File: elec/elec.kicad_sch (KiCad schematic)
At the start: 14 parts, among them J1 BM04B-SRSS-TB, J10 BM04B-SRSS-TB, J11 DB301V-3.5-2P-GN-S, J2 BM04B-SRSS-TB, J3 BM04B-SRSS-TB, J4 BM04B-SRSS-TB, J5 BM04B-SRSS-TB, J6 BM04B-SRSS-TB, J7 BM04B-SRSS-TB, J8 BM04B-SRSS-TB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

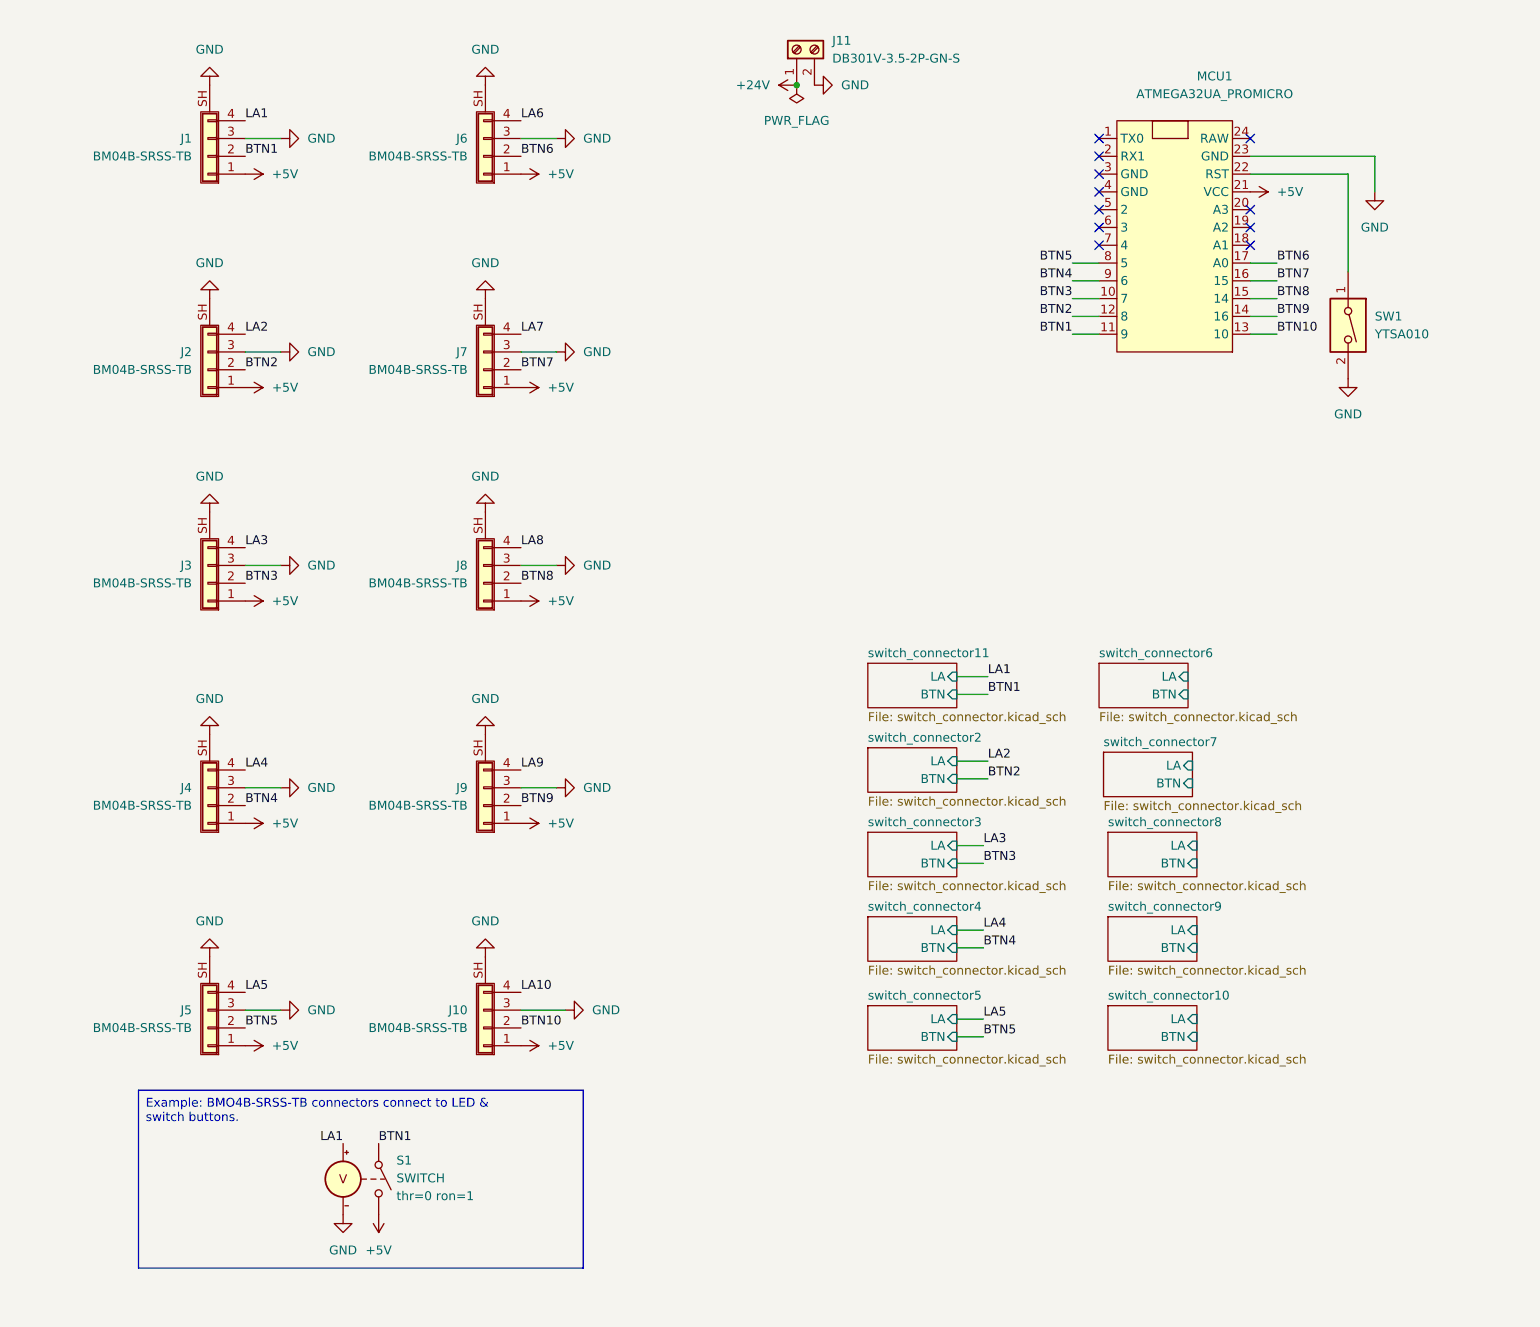
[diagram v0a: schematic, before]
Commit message: feat: adding modularity to PCB
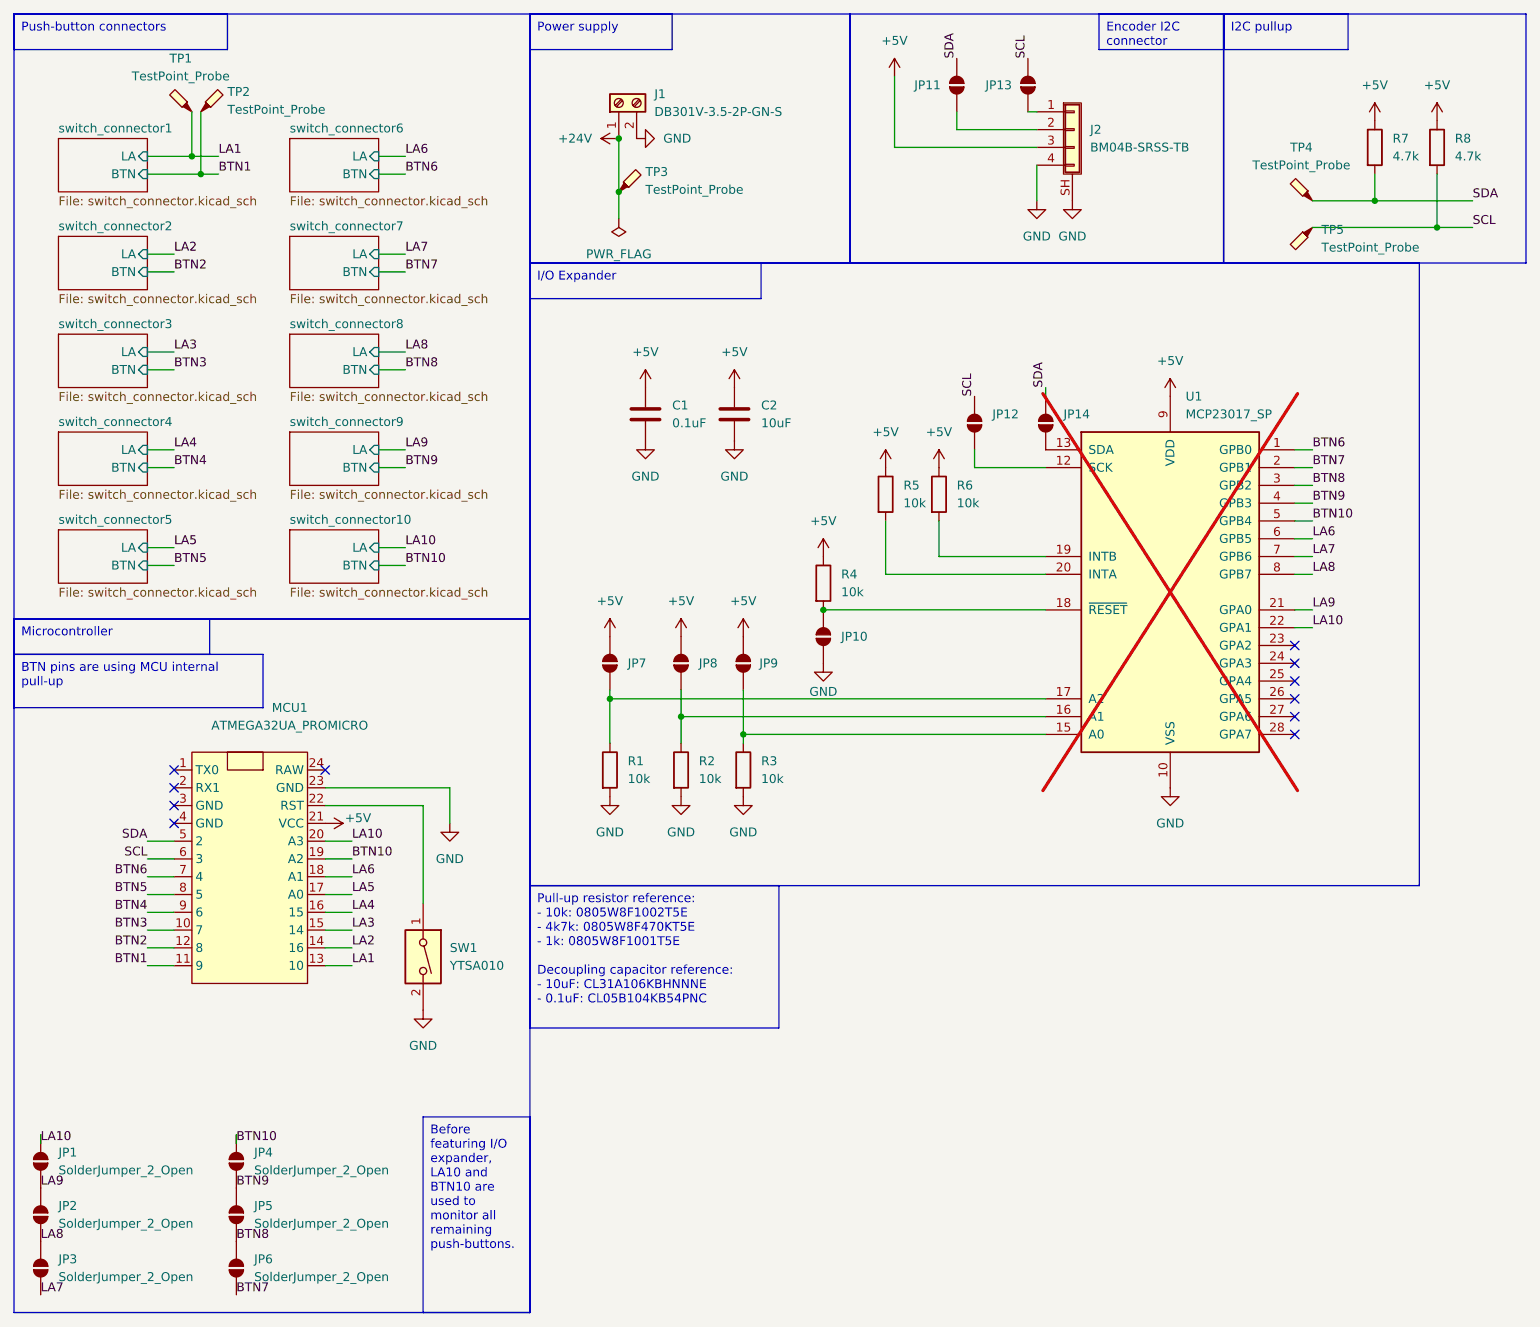
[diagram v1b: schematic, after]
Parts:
- removed J1, J10, J3, J4, J5, J6, J7, J8, J9: BM04B-SRSS-TB, jlcpcb:JST_SH_BM04B-SRSS-TB_1x04-1MP_P1.00mm_Vertical, symbol Connector_Generic_Shielded:Conn_01x04_Shielded
- removed S1: SWITCH, symbol Simulation_SPICE:SWITCH
- added C1: 0.1uF, Capacitor_SMD:C_0402_1005Metric, symbol Device:C
- added C2: 10uF, Capacitor_SMD:C_1206_3216Metric, symbol Device:C
- added JP1, JP10, JP12, JP13, JP14, JP2, JP3, JP4, JP5, JP6, JP7, JP8, JP9: SolderJumper_2_Open, Jumper:SolderJumper-2_P1.3mm_Open_Pad1.0x1.5mm, symbol Jumper:SolderJumper_2_Open
- added JP11: SolderJumper_2_Open, Jumper:SolderJumper-2_P1.3mm_Bridged_Pad1.0x1.5mm, symbol Jumper:SolderJumper_2_Open
- added R1, R2, R3, R4, R5, R6: 10k, Resistor_SMD:R_0805_2012Metric, symbol Device:R
- added R7, R8: 4.7k, Resistor_SMD:R_0805_2012Metric, symbol Device:R
- added TP1, TP2, TP3, TP4, TP5: TestPoint_Probe, TestPoint:TestPoint_THTPad_D3.0mm_Drill1.5mm, symbol Connector:TestPoint_Probe
- added U1: MCP23017_SP, Package_DIP:DIP-28_W7.62mm, symbol Interface_Expansion:MCP23017_SP
- renumbered J11 to J1
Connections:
- net +24V: now also TP3.1
- net +5V: now also J2.3 (Pin_3), C1.1, C2.1, JP7.1 (A), JP8.1 (A), JP9.1 (A), R4.1, R5.1, R6.1, R7.1, R8.1, U1.9 (VDD); no longer J2.1 (Pin_1)
- net BTN1: now also TP2.1
- net BTN10: now also MCU1.19 (A2), JP4.2 (B), U1.5 (GPB4); no longer MCU1.13 (10)
- net BTN2: no longer J2.2 (Pin_2)
- net BTN6: now also MCU1.7 (4), U1.1 (GPB0); no longer MCU1.17 (A0)
- net BTN7: now also JP6.1 (A), U1.2 (GPB1); no longer MCU1.16 (15)
- net BTN8: now also JP5.2 (B), JP6.2 (B), U1.3 (GPB2); no longer MCU1.15 (14)
- net BTN9: now also JP4.1 (A), JP5.1 (A), U1.4 (GPB3); no longer MCU1.14 (16)
- net GND: now also J2.4 (Pin_4), C1.2, C2.2, JP10.1 (A), R1.2, R2.2, R3.2, U1.10 (VSS); no longer J2.3 (Pin_3)
- net LA1: now also MCU1.13 (10), TP1.1
- net LA10: now also MCU1.20 (A3), JP1.2 (B), U1.22 (GPA1)
- net LA2: now also MCU1.14 (16); no longer J2.4 (Pin_4)
- net LA3: now also MCU1.15 (14)
- net LA4: now also MCU1.16 (15)
- net LA5: now also MCU1.17 (A0)
- net LA6: now also MCU1.18 (A1), U1.6 (GPB5)
- net LA7: now also JP3.1 (A), U1.7 (GPB6)
- net LA8: now also JP2.2 (B), JP3.2 (B), U1.8 (GPB7)
- net LA9: now also JP1.1 (A), JP2.1 (A), U1.21 (GPA0)
- net SDA: now reaches MCU1.5 (2)
- net SDA: now also JP11.2 (B), JP14.1 (A), R7.2, TP4.1
- net SCL: now reaches MCU1.6 (3)
- net SCL: now also JP12.2 (B), JP13.2 (B), R8.2, TP5.1
- new net: J2.1 (Pin_1), JP13.1 (A)
- new net: J2.2 (Pin_2), JP11.1 (A)
- new net: JP9.2 (B), R3.1, U1.15 (A0)
- new net: JP10.2 (B), R4.2, U1.18 (~{RESET})
- new net: JP12.1 (A), U1.12 (SCK)
- new net: JP14.2 (B), U1.13 (SDA)
- new net: JP8.2 (B), R2.1, U1.16 (A1)
- new net: JP7.2 (B), R1.1, U1.17 (A2)
- new net: R6.2, U1.19 (INTB)
- new net: R5.2, U1.20 (INTA)
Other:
- removed sheet switch_connector11
- added sheet switch_connector1 (switch_connector.kicad_sch)
- moved on the sheet: J1, MCU1, SW1

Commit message: v1 3D print PCB
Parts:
- renumbered JP6 to JP4, JP4 to JP5, JP5 to JP6
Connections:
- net +24V: now also J1.2 (Pin_2); no longer J1.1 (Pin_1)
- net BTN1: now also MCU1.14 (16); no longer MCU1.11 (9)
- net BTN10: now also MCU1.8 (5), U1.22 (GPA1); no longer MCU1.19 (A2), U1.5 (GPB4)
- net BTN2: now also MCU1.16 (15); no longer MCU1.12 (8)
- net BTN3: now also MCU1.18 (A1); no longer MCU1.10 (7)
- net BTN4: now also MCU1.20 (A3); no longer MCU1.9 (6)
- net BTN5: now also MCU1.11 (9); no longer MCU1.8 (5)
- net BTN6: now also MCU1.10 (7), U1.2 (GPB1); no longer MCU1.7 (4), U1.1 (GPB0)
- net BTN7: now also MCU1.9 (6), U1.28 (GPA7); no longer JP4.1 (A), U1.2 (GPB1)
- net BTN8: now also U1.26 (GPA5); no longer JP4.2 (B), U1.3 (GPB2)
- net BTN9: now also U1.24 (GPA3); no longer U1.4 (GPB3)
- net GND: now also J1.1 (Pin_1), MCU1.3 (GND), MCU1.4 (GND); no longer J1.2 (Pin_2)
- net LA10: now also MCU1.7 (4), U1.21 (GPA0); no longer MCU1.20 (A3), U1.22 (GPA1)
- net LA2: now also MCU1.15 (14); no longer MCU1.14 (16)
- net LA3: now also MCU1.17 (A0); no longer MCU1.15 (14)
- net LA4: now also MCU1.19 (A2); no longer MCU1.16 (15)
- net LA5: now also MCU1.12 (8); no longer MCU1.17 (A0)
- net LA6: now also JP4.1 (A), U1.1 (GPB0); no longer MCU1.18 (A1), U1.6 (GPB5)
- net LA7: now also JP4.2 (B), U1.27 (GPA6); no longer U1.7 (GPB6)
- net LA8: now also U1.25 (GPA4); no longer U1.8 (GPB7)
- net LA9: now also U1.23 (GPA2); no longer U1.21 (GPA0)
- no-connect marks 11 -> 9
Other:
- moved on the sheet: J1, JP1, JP2, JP3, JP4, JP5, JP6, R7, R8, TP3, TP4, TP5

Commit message: doc: outline for fabrication guide
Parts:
- C1: MPN (none) -> C307331
- C2: MPN (none) -> C13585
- J1: value DB301V-3.5-2P-GN-S -> Screw terminal; MPN (none) -> C695629
- J2: MPN (none) -> C160390
- JP11: footprint Jumper:SolderJumper-2_P1.3mm_Bridged_Pad1.0x1.5mm -> Jumper:SolderJumper-2_P1.3mm_Open_Pad1.0x1.5mm
- MCU1, TP1, TP2, TP3, TP4, TP5: now not fitted
- R1, R2, R3, R4, R5: MPN (none) -> C17414
- R6: jMPN (none) -> C17414
- R7, R8: MPN (none) -> C17675
- SW1: MPN (none) -> C2910844
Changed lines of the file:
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@@
 		)
 	)
-	(text_box "Pull-up resistor reference:\n- 10k: 0805W8F1002T5E\n- 4k7k: 0805W8F470KT5E\n- 1k: 0805W8F1001T5E\n\nDecoupling capacitor reference:\n- 10uF: CL31A106KBHNNNE\n- 0.1uF: CL05B104KB54PNC"
-		(exclude_from_sim no)
-		(at 86.36 137.16 0)
-		(size 35.56 20.32)
-		(stroke
-			(width 0)
-			(type default)
-		)
-		(fill
-			(type none)
-		)
-		(effects
-			(font
-				(size 1.27 1.27)
-			)
-			(justify left top)
-		)
-	)
 	(label "BTN10"
 		(at 198.12 100.33 0)
@@
 		(in_bom yes)
 		(on_board yes)
-		(dnp no)
+		(dnp yes)
 		(fields_autoplaced yes)
 		(property "Reference" "TP1"
@@
 			)
 		)
+		(property "MPN" "C160390"
+			(at 163.83 29.21 0)
+			(effects
+				(font
+					(size 1.27 1.27)
+				)
+				(hide yes)
+			)
+		)
 		(pin "3"
 		)
@@
 			)
 		)
+		(property "MPN" "C17675"
+			(at 208.28 26.67 0)
+			(effects
+				(font
+					(size 1.27 1.27)
+				)
+				(hide yes)
+			)
+		)
 		(pin "1"
 		)
@@
 			)
 		)
+		(property "MPN" "C17414"
+			(at 116.84 120.65 0)
+			(effects
+				(font
+					(size 1.27 1.27)
+				)
+				(hide yes)
+			)
+		)
 		(pin "1"
 		)
@@
 			)
 		)
-		(property "Value" "DB301V-3.5-2P-GN-S"
+		(property "Value" "Screw terminal"
 			(at 97.79 29.21 0)
 			(effects
@@
 			)
 		)
+		(property "MPN" "C695629"
+			(at 97.79 35.56 0)
+			(effects
+				(font
+					(size 1.27 1.27)
+				)
+				(hide yes)
+			)
+		)
 		(pin "1"
 		)
@@
 			)
 		)
+		(property "MPN" "C13585"
+			(at 115.57 69.85 0)
+			(effects
+				(font
+					(size 1.27 1.27)
+				)
+				(hide yes)
+			)
+		)
 		(pin "1"
 		)
@@
 		(in_bom yes)
 		(on_board yes)
-		(dnp no)
+		(dnp yes)
 		(fields_autoplaced yes)
 		(property "Reference" "MCU1"
@@
 		(in_bom yes)
 		(on_board yes)
-		(dnp no)
+		(dnp yes)
 		(fields_autoplaced yes)
 		(property "Reference" "TP3"
@@
 			)
 		)
-		(property "Footprint" "Jumper:SolderJumper-2_P1.3mm_Bridged_Pad1.0x1.5mm"
+		(property "Footprint" "Jumper:SolderJumper-2_P1.3mm_Open_Pad1.0x1.5mm"
 			(at 147.32 22.86 0)
 			(effects
@@
 			)
 		)
+		(property "jMPN" "C17414"
+			(at 144.78 81.28 0)
+			(effects
+				(font
+					(size 1.27 1.27)
+				)
+				(hide yes)
+			)
+		)
 		(pin "2"
 		)
@@
 		(in_bom yes)
 		(on_board yes)
-		(dnp no)
+		(dnp yes)
 		(fields_autoplaced yes)
 		(property "Reference" "TP4"
@@
 			)
 		)
+		(property "MPN" "C17414"
+			(at 97.79 120.65 0)
+			(effects
+				(font
+					(size 1.27 1.27)
+				)
+				(hide yes)
+			)
+		)
 		(pin "1"
 		)
@@
 		(in_bom yes)
 		(on_board yes)
-		(dnp no)
+		(dnp yes)
 		(fields_autoplaced yes)
 		(property "Reference" "TP5"
@@
 			)
 		)
+		(property "MPN" "C307331"
+			(at 102.87 69.85 0)
+			(effects
+				(font
+					(size 1.27 1.27)
+				)
+				(hide yes)
+			)
+		)
 		(pin "2"
 		)
@@
 			)
 		)
+		(property "MPN" "C17414"
+			(at 137.16 81.28 0)
+			(effects
+				(font
+					(size 1.27 1.27)
+				)
+				(hide yes)
+			)
+		)
 		(pin "2"
 		)
@@
 			)
 		)
+		(property "MPN" "C2910844"
+			(at 71.12 147.32 90)
+			(effects
+				(font
+					(size 1.27 1.27)
+				)
+				(hide yes)
+			)
+		)
 		(pin "2"
 		)
@@
 			)
 		)
+		(property "MPN" "C17675"
+			(at 217.17 26.67 0)
+			(effects
+				(font
+					(size 1.27 1.27)
+				)
+				(hide yes)
+			)
+		)
 		(pin "1"
 		)
@@
 			)
 		)
+		(property "MPN" "C17414"
+			(at 128.27 93.98 0)
+			(effects
+				(font
+					(size 1.27 1.27)
+				)
+				(hide yes)
+			)
+		)
 		(pin "2"
 		)
@@
 			)
 		)
+		(property "MPN" "C17414"
+			(at 107.95 120.65 0)
+			(effects
+				(font
+					(size 1.27 1.27)
+				)
+				(hide yes)
+			)
+		)
 		(pin "1"
 		)
@@
 		(in_bom yes)
 		(on_board yes)
-		(dnp no)
+		(dnp yes)
 		(fields_autoplaced yes)
 		(property "Reference" "TP2"

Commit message: main - feat: updating delivrables
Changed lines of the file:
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@@
 		)
 	)
-	(label "BTN5"
+	(label "LA5"
 		(at 31.75 148.59 180)
 		(fields_autoplaced yes)
@@
 		)
 	)
-	(label "LA5"
+	(label "BTN5"
 		(at 31.75 146.05 180)
 		(fields_autoplaced yes)
